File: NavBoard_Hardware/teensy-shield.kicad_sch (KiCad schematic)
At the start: 6 parts, among them J3 Conn_01x24, J4 Conn_01x24, J5 Conn_01x06, J6 Conn_01x24, J7 Conn_01x24, U5 Teensy4.1

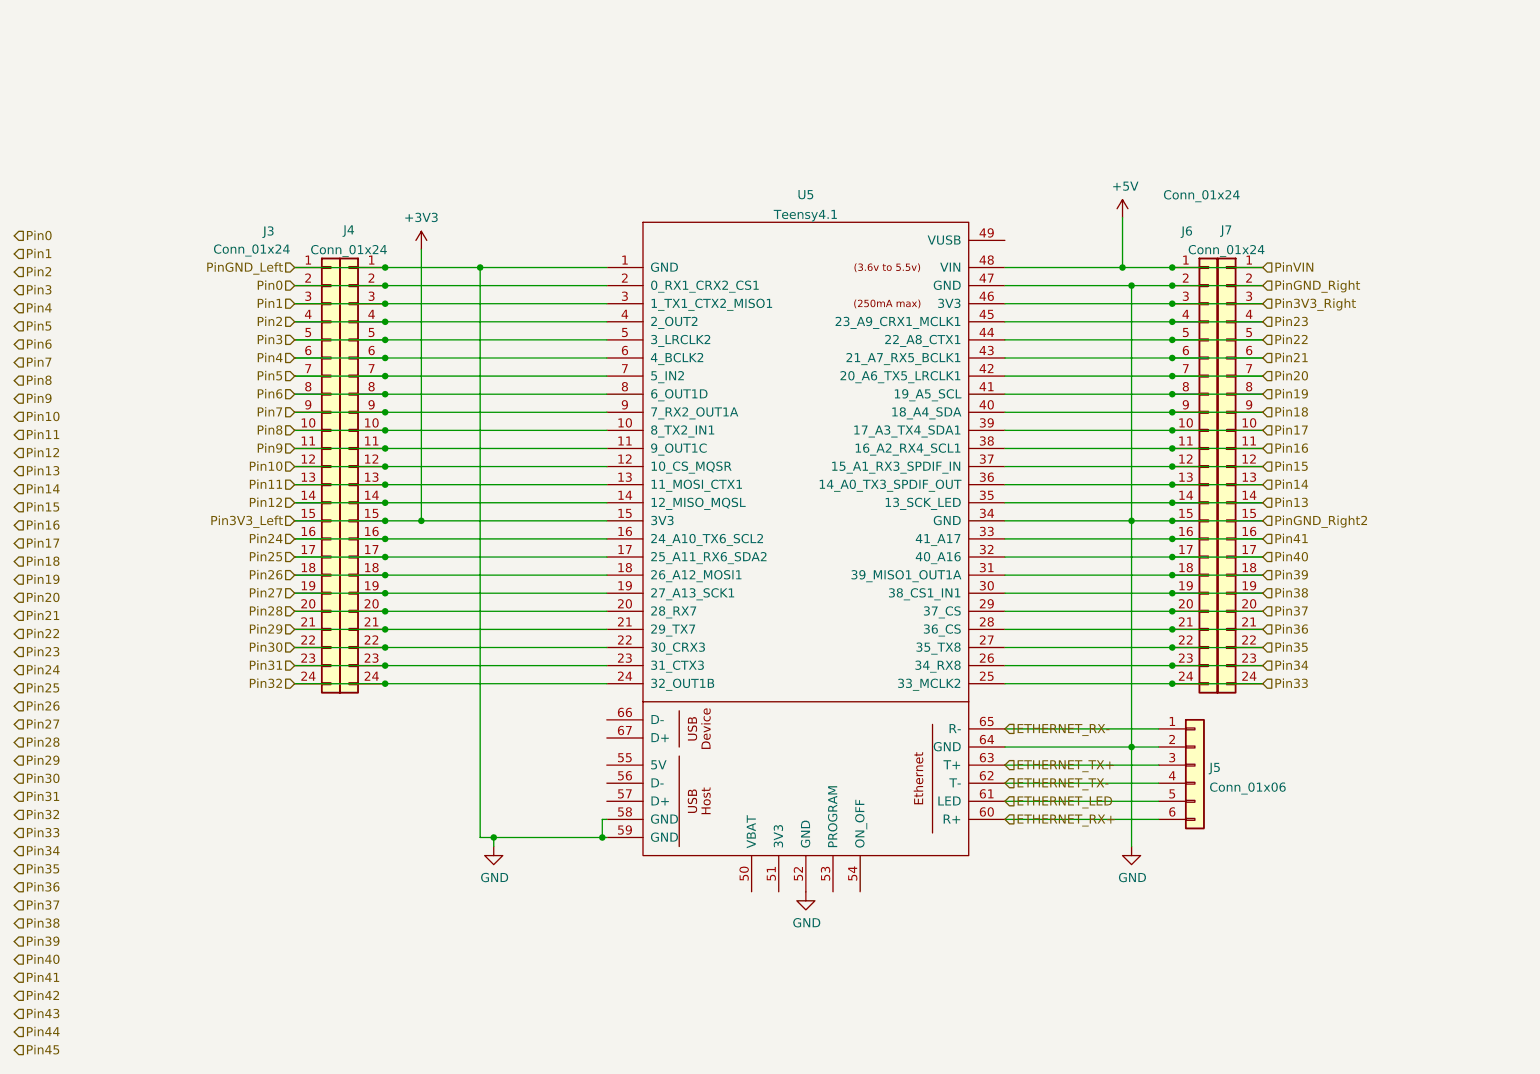
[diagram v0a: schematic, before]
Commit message: Created adapter symbols and footprints
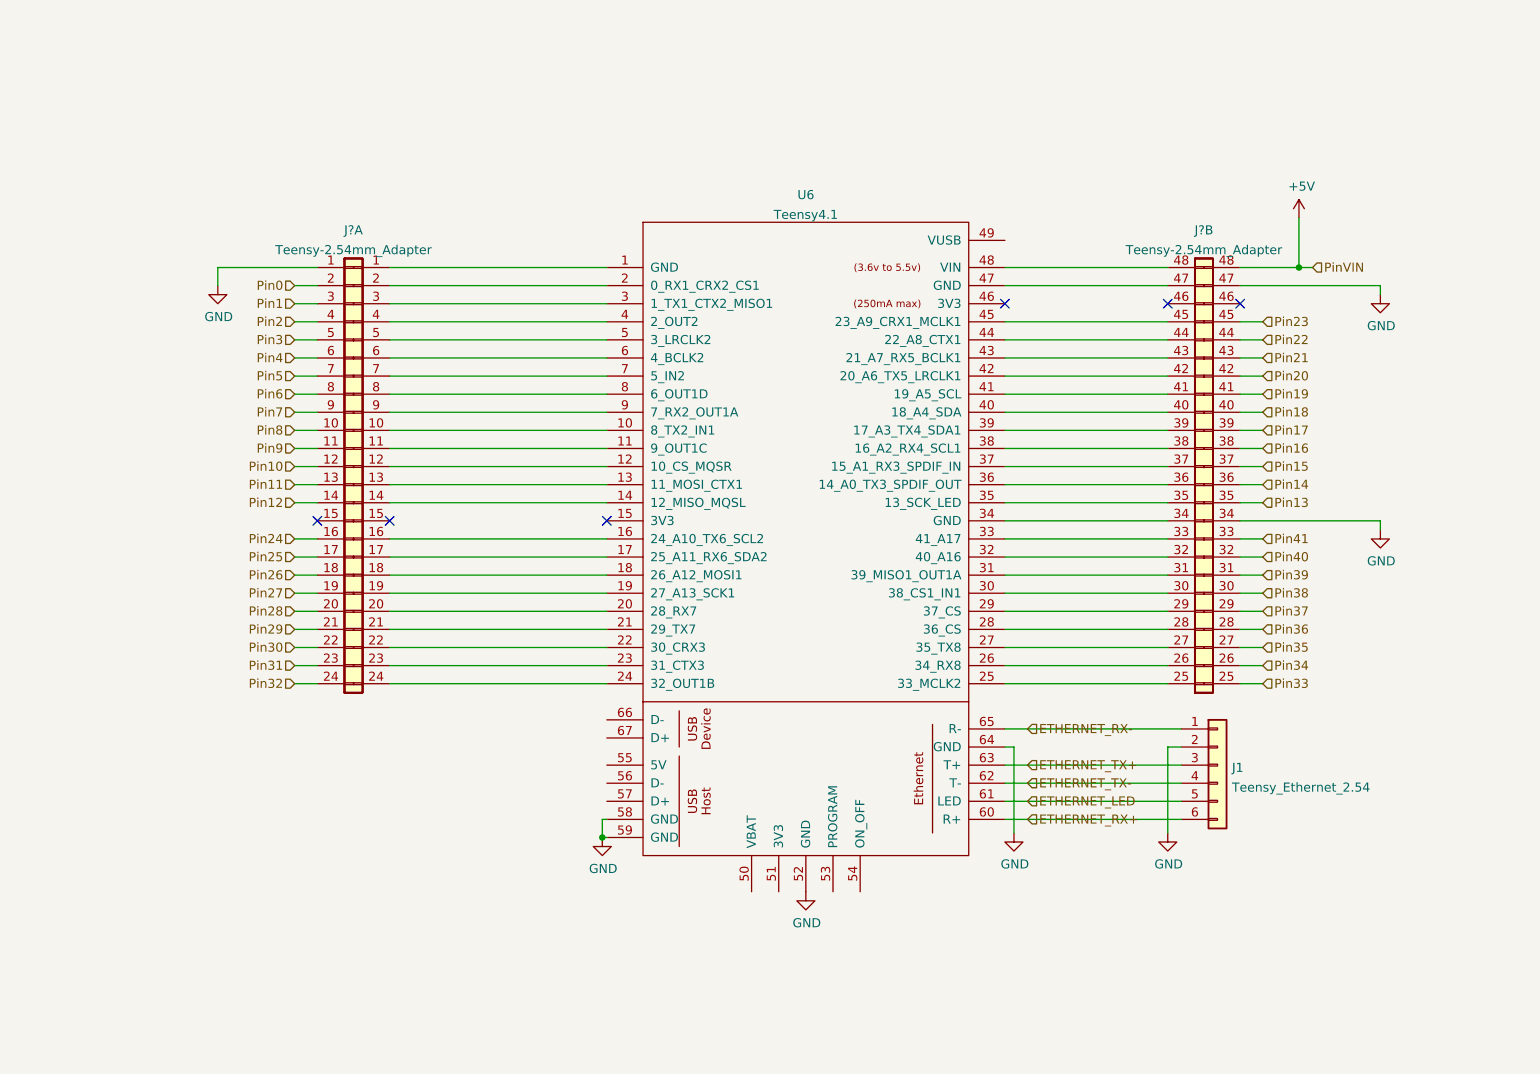
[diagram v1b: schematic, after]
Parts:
- removed J3, J4, J6, J7: Conn_01x24, symbol Connector_Generic:Conn_01x24
- added J? (x2): Teensy-2.54mm_Adapter, Nav_Board:Teensy-2.54mm_Adapter, symbol Nav_Board:Teensy-2.54mm_Adapter
- J1: renamed from J5; value Conn_01x06 -> Teensy_Ethernet_2.54
- renumbered U5 to U6
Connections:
- net +5V: now also J?.48; no longer U6.48 (VIN)
- net GND: now also J?.1, J?.34, J?.47; no longer U6.1 (GND), U6.34 (GND), U6.47 (GND)
- net Pin0: now also J?.2; no longer U6.2 (0_RX1_CRX2_CS1)
- net Pin1: now also J?.3; no longer U6.3 (1_TX1_CTX2_MISO1)
- net Pin10: now also J?.12; no longer U6.12 (10_CS_MQSR)
- net Pin11: now also J?.13; no longer U6.13 (11_MOSI_CTX1)
- net Pin12: now also J?.14; no longer U6.14 (12_MISO_MQSL)
- net Pin13: now also J?.35; no longer U6.35 (13_SCK_LED)
- net Pin14: now also J?.36; no longer U6.36 (14_A0_TX3_SPDIF_OUT)
- net Pin15: now also J?.37; no longer U6.37 (15_A1_RX3_SPDIF_IN)
- net Pin16: now also J?.38; no longer U6.38 (16_A2_RX4_SCL1)
- net Pin17: now also J?.39; no longer U6.39 (17_A3_TX4_SDA1)
- net Pin18: now also J?.40; no longer U6.40 (18_A4_SDA)
- net Pin19: now also J?.41; no longer U6.41 (19_A5_SCL)
- net Pin2: now also J?.4; no longer U6.4 (2_OUT2)
- net Pin20: now also J?.42; no longer U6.42 (20_A6_TX5_LRCLK1)
- net Pin21: now also J?.43; no longer U6.43 (21_A7_RX5_BCLK1)
- net Pin22: now also J?.44; no longer U6.44 (22_A8_CTX1)
- net Pin23: now also J?.45; no longer U6.45 (23_A9_CRX1_MCLK1)
- net Pin24: now also J?.16; no longer U6.16 (24_A10_TX6_SCL2)
- net Pin25: now also J?.17; no longer U6.17 (25_A11_RX6_SDA2)
- net Pin26: now also J?.18; no longer U6.18 (26_A12_MOSI1)
- net Pin27: now also J?.19; no longer U6.19 (27_A13_SCK1)
- net Pin28: now also J?.20; no longer U6.20 (28_RX7)
- net Pin29: now also J?.21; no longer U6.21 (29_TX7)
- net Pin3: now also J?.5; no longer U6.5 (3_LRCLK2)
- net Pin30: now also J?.22; no longer U6.22 (30_CRX3)
- net Pin31: now also J?.23; no longer U6.23 (31_CTX3)
- net Pin32: now also J?.24; no longer U6.24 (32_OUT1B)
- net Pin33: now also J?.25; no longer U6.25 (33_MCLK2)
- net Pin34: now also J?.26; no longer U6.26 (34_RX8)
- net Pin35: now also J?.27; no longer U6.27 (35_TX8)
- net Pin36: now also J?.28; no longer U6.28 (36_CS)
- net Pin37: now also J?.29; no longer U6.29 (37_CS)
- net Pin38: now also J?.30; no longer U6.30 (38_CS1_IN1)
- net Pin39: now also J?.31; no longer U6.31 (39_MISO1_OUT1A)
- net Pin4: now also J?.6; no longer U6.6 (4_BCLK2)
- net Pin40: now also J?.32; no longer U6.32 (40_A16)
- net Pin41: now also J?.33; no longer U6.33 (41_A17)
- net Pin5: now also J?.7; no longer U6.7 (5_IN2)
- net Pin6: now also J?.8; no longer U6.8 (6_OUT1D)
- net Pin7: now also J?.9; no longer U6.9 (7_RX2_OUT1A)
- net Pin8: now also J?.10; no longer U6.10 (8_TX2_IN1)
- net Pin9: now also J?.11; no longer U6.11 (9_OUT1C)
- net +3V3: no longer names the net of U6.15 (3V3)
- net Pin3V3_Right: no longer names the net of U6.46 (3V3)
- new net: J?.1, U6.1 (GND)
- new net: J?.10, U6.10 (8_TX2_IN1)
- new net: J?.11, U6.11 (9_OUT1C)
- new net: J?.12, U6.12 (10_CS_MQSR)
- new net: J?.13, U6.13 (11_MOSI_CTX1)
- new net: J?.14, U6.14 (12_MISO_MQSL)
- new net: J?.16, U6.16 (24_A10_TX6_SCL2)
- new net: J?.17, U6.17 (25_A11_RX6_SDA2)
- new net: J?.18, U6.18 (26_A12_MOSI1)
- new net: J?.19, U6.19 (27_A13_SCK1)
- new net: J?.2, U6.2 (0_RX1_CRX2_CS1)
- new net: J?.20, U6.20 (28_RX7)
- new net: J?.21, U6.21 (29_TX7)
- new net: J?.22, U6.22 (30_CRX3)
- new net: J?.23, U6.23 (31_CTX3)
- new net: J?.24, U6.24 (32_OUT1B)
- new net: J?.25, U6.25 (33_MCLK2)
- new net: J?.26, U6.26 (34_RX8)
- new net: J?.27, U6.27 (35_TX8)
- new net: J?.28, U6.28 (36_CS)
- new net: J?.29, U6.29 (37_CS)
- new net: J?.3, U6.3 (1_TX1_CTX2_MISO1)
- new net: J?.30, U6.30 (38_CS1_IN1)
- new net: J?.31, U6.31 (39_MISO1_OUT1A)
- new net: J?.32, U6.32 (40_A16)
- new net: J?.33, U6.33 (41_A17)
- new net: J?.34, U6.34 (GND)
- new net: J?.35, U6.35 (13_SCK_LED)
- new net: J?.36, U6.36 (14_A0_TX3_SPDIF_OUT)
- new net: J?.37, U6.37 (15_A1_RX3_SPDIF_IN)
- new net: J?.38, U6.38 (16_A2_RX4_SCL1)
- new net: J?.39, U6.39 (17_A3_TX4_SDA1)
- new net: J?.4, U6.4 (2_OUT2)
- new net: J?.40, U6.40 (18_A4_SDA)
- new net: J?.41, U6.41 (19_A5_SCL)
- new net: J?.42, U6.42 (20_A6_TX5_LRCLK1)
- new net: J?.43, U6.43 (21_A7_RX5_BCLK1)
- new net: J?.44, U6.44 (22_A8_CTX1)
- new net: J?.45, U6.45 (23_A9_CRX1_MCLK1)
- new net: J?.47, U6.47 (GND)
- new net: J?.48, U6.48 (VIN)
- new net: J?.5, U6.5 (3_LRCLK2)
- new net: J?.6, U6.6 (4_BCLK2)
- new net: J?.7, U6.7 (5_IN2)
- new net: J?.8, U6.8 (6_OUT1D)
- new net: J?.9, U6.9 (7_RX2_OUT1A)
- no-connect marks 0 -> 6
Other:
- moved on the sheet: J1

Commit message: Added connectors, cleaned up file directory
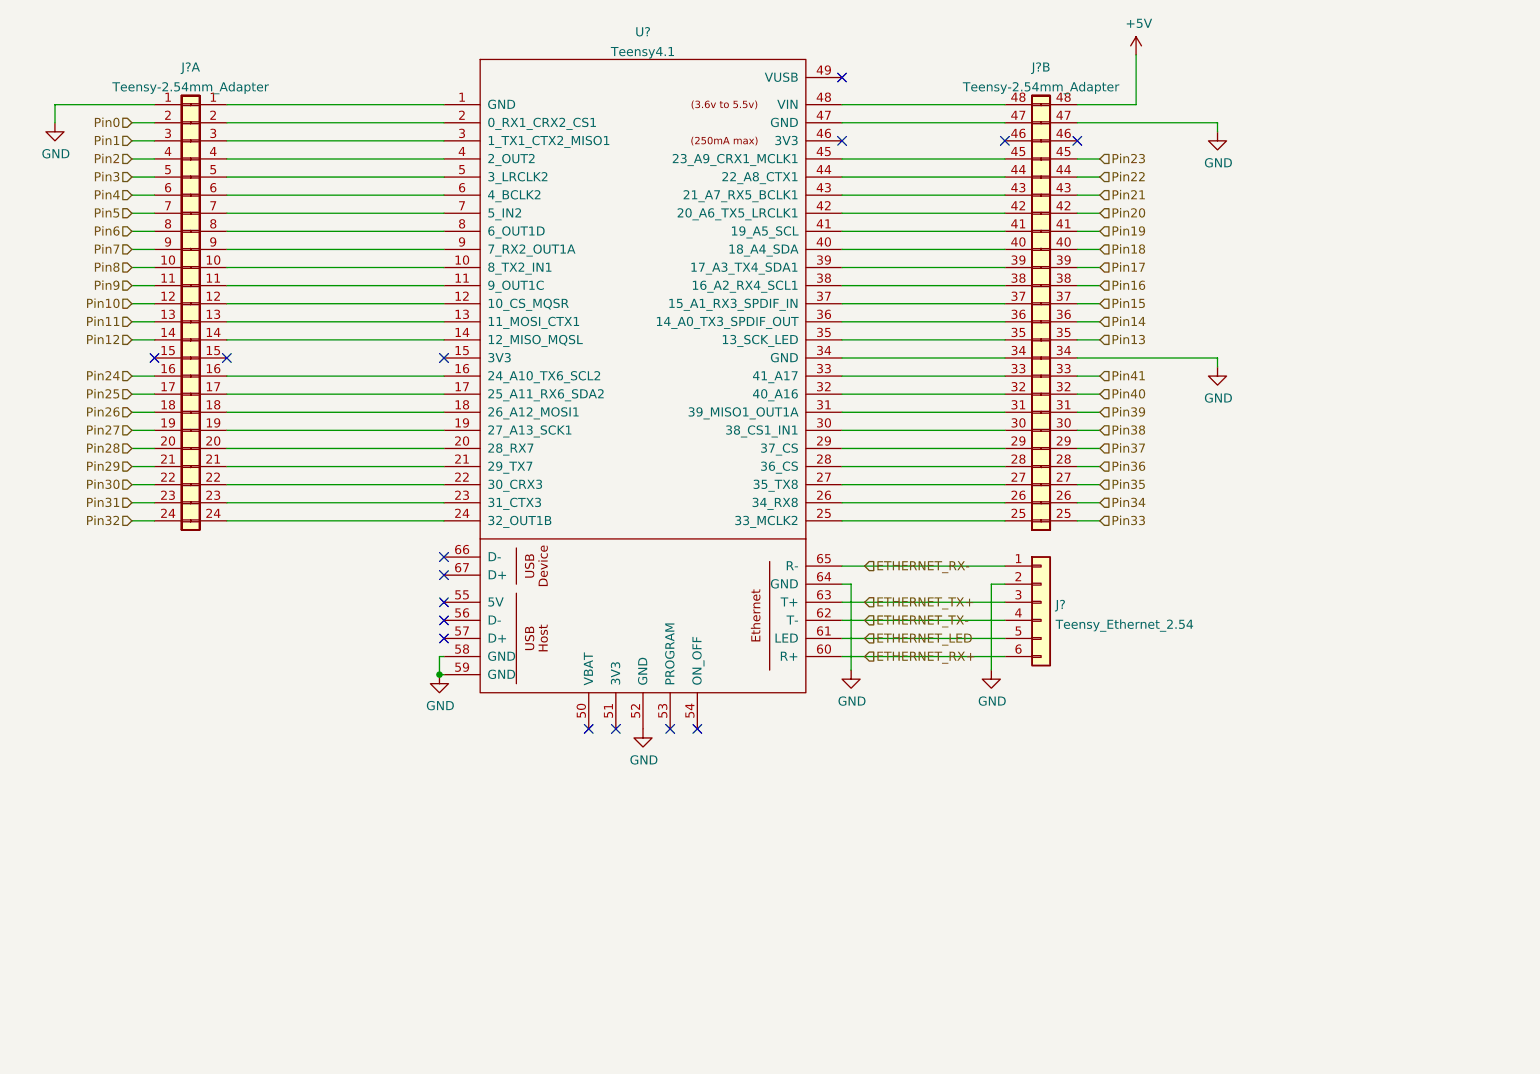
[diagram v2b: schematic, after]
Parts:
- removed J? (x2): Teensy-2.54mm_Adapter, Nav_Board:Teensy-2.54mm_Adapter, symbol Nav_Board:Teensy-2.54mm_Adapter
- added J? (x2): Teensy-2.54mm_Adapter, Nav_Board:Teensy-2.54mm_Adapter, symbol Nav_Board:Teensy-2.54mm_Adapter
- renumbered J1 to J?, U6 to U?
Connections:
- net +5V: now also J?.48
- net GND: now also J?.1, J?.34, J?.47
- net Pin0: now also J?.2
- net Pin1: now also J?.3
- net Pin10: now also J?.12
- net Pin11: now also J?.13
- net Pin12: now also J?.14
- net Pin13: now also J?.35
- net Pin14: now also J?.36
- net Pin15: now also J?.37
- net Pin16: now also J?.38
- net Pin17: now also J?.39
- net Pin18: now also J?.40
- net Pin19: now also J?.41
- net Pin2: now also J?.4
- net Pin20: now also J?.42
- net Pin21: now also J?.43
- net Pin22: now also J?.44
- net Pin23: now also J?.45
- net Pin24: now also J?.16
- net Pin25: now also J?.17
- net Pin26: now also J?.18
- net Pin27: now also J?.19
- net Pin28: now also J?.20
- net Pin29: now also J?.21
- net Pin3: now also J?.5
- net Pin30: now also J?.22
- net Pin31: now also J?.23
- net Pin32: now also J?.24
- net Pin33: now also J?.25
- net Pin34: now also J?.26
- net Pin35: now also J?.27
- net Pin36: now also J?.28
- net Pin37: now also J?.29
- net Pin38: now also J?.30
- net Pin39: now also J?.31
- net Pin4: now also J?.6
- net Pin40: now also J?.32
- net Pin41: now also J?.33
- net Pin5: now also J?.7
- net Pin6: now also J?.8
- net Pin7: now also J?.9
- net Pin8: now also J?.10
- net Pin9: now also J?.11
- net at U?.1 (GND): now also J?.1
- net at U?.10 (8_TX2_IN1): now also J?.10
- net at U?.11 (9_OUT1C): now also J?.11
- net at U?.12 (10_CS_MQSR): now also J?.12
- net at U?.13 (11_MOSI_CTX1): now also J?.13
- net at U?.14 (12_MISO_MQSL): now also J?.14
- net at U?.16 (24_A10_TX6_SCL2): now also J?.16
- net at U?.17 (25_A11_RX6_SDA2): now also J?.17
- net at U?.18 (26_A12_MOSI1): now also J?.18
- net at U?.19 (27_A13_SCK1): now also J?.19
- net at U?.2 (0_RX1_CRX2_CS1): now also J?.2
- net at U?.20 (28_RX7): now also J?.20
- net at U?.21 (29_TX7): now also J?.21
- net at U?.22 (30_CRX3): now also J?.22
- net at U?.23 (31_CTX3): now also J?.23
- net at U?.24 (32_OUT1B): now also J?.24
- net at U?.25 (33_MCLK2): now also J?.25
- net at U?.26 (34_RX8): now also J?.26
- net at U?.27 (35_TX8): now also J?.27
- net at U?.28 (36_CS): now also J?.28
- net at U?.29 (37_CS): now also J?.29
- net at U?.3 (1_TX1_CTX2_MISO1): now also J?.3
- net at U?.30 (38_CS1_IN1): now also J?.30
- net at U?.31 (39_MISO1_OUT1A): now also J?.31
- net at U?.32 (40_A16): now also J?.32
- net at U?.33 (41_A17): now also J?.33
- net at U?.34 (GND): now also J?.34
- net at U?.35 (13_SCK_LED): now also J?.35
- net at U?.36 (14_A0_TX3_SPDIF_OUT): now also J?.36
- net at U?.37 (15_A1_RX3_SPDIF_IN): now also J?.37
- net at U?.38 (16_A2_RX4_SCL1): now also J?.38
- net at U?.39 (17_A3_TX4_SDA1): now also J?.39
- net at U?.4 (2_OUT2): now also J?.4
- net at U?.40 (18_A4_SDA): now also J?.40
- net at U?.41 (19_A5_SCL): now also J?.41
- net at U?.42 (20_A6_TX5_LRCLK1): now also J?.42
- net at U?.43 (21_A7_RX5_BCLK1): now also J?.43
- net at U?.44 (22_A8_CTX1): now also J?.44
- net at U?.45 (23_A9_CRX1_MCLK1): now also J?.45
- net at U?.47 (GND): now also J?.47
- net at U?.48 (VIN): now also J?.48
- net at U?.5 (3_LRCLK2): now also J?.5
- net at U?.6 (4_BCLK2): now also J?.6
- net at U?.7 (5_IN2): now also J?.7
- net at U?.8 (6_OUT1D): now also J?.8
- net at U?.9 (7_RX2_OUT1A): now also J?.9
- no-connect marks 6 -> 16
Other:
- moved on the sheet: J?, U?

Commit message: Most schematic connections completed
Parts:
- J?: Inner Type (none) -> 2.54mm Sockets; Outer Type (none) -> 2.54mm Pins
- J?: Inner Type (none) -> 2.54mm Sockets; Outer Types (none) -> 2.54mm Pins
- U?: Left Headers (none) -> 2.54mm Pins; Right Headers (none) -> 2.54mm Pins
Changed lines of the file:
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@@
   )
   (symbol (lib_id "Nav_Board:Teensy-2.54mm_Adapter") (at 205.105 48.895 0) (unit 2)
-    (in_bom yes) (on_board yes) (fields_autoplaced)
+    (in_bom yes) (on_board yes)
     (property "Reference" "J?" (id 0) (at 205.105 44.9285 0))
     (property "Value" "Teensy-2.54mm_Adapter" (id 1) (at 205.105 47.7036 0))
@@
       (effects (font (size 1.27 1.27)) hide)
     )
+    (property "Inner Type" "2.54mm Sockets" (id 4) (at 194.945 111.76 0))
+    (property "Outer Type" "2.54mm Pins" (id 5) (at 213.995 111.76 0))
     (pin "25")
     (pin "25")
@@
   )
   (symbol (lib_id "Nav_Board:Teensy-2.54mm_Adapter") (at 85.725 48.895 0) (unit 1)
-    (in_bom yes) (on_board yes) (fields_autoplaced)
+    (in_bom yes) (on_board yes)
     (property "Reference" "J?" (id 0) (at 85.725 44.9285 0))
     (property "Value" "Teensy-2.54mm_Adapter" (id 1) (at 85.725 47.7036 0))
@@
       (effects (font (size 1.27 1.27)) hide)
     )
+    (property "Inner Type" "2.54mm Sockets" (id 4) (at 95.885 111.76 0))
+    (property "Outer Types" "2.54mm Pins" (id 5) (at 77.47 111.76 0))
     (pin "1")
     (pin "1")
@@
   )
   (symbol (lib_id "teensy:Teensy4.1") (at 149.225 104.775 0) (unit 1)
-    (in_bom yes) (on_board yes) (fields_autoplaced)
+    (in_bom yes) (on_board yes)
     (property "Reference" "U?" (id 0) (at 149.225 39.9755 0))
     (property "Value" "Teensy4.1" (id 1) (at 149.225 42.7506 0))
@@
       (effects (font (size 1.27 1.27)) hide)
     )
+    (property "Left Headers" "2.54mm Pins" (id 4) (at 126.365 41.275 0))
+    (property "Right Headers" "2.54mm Pins" (id 5) (at 172.085 41.275 0))
     (pin "10")
     (pin "11")
